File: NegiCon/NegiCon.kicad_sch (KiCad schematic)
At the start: 1 part, among them U4 SC0915

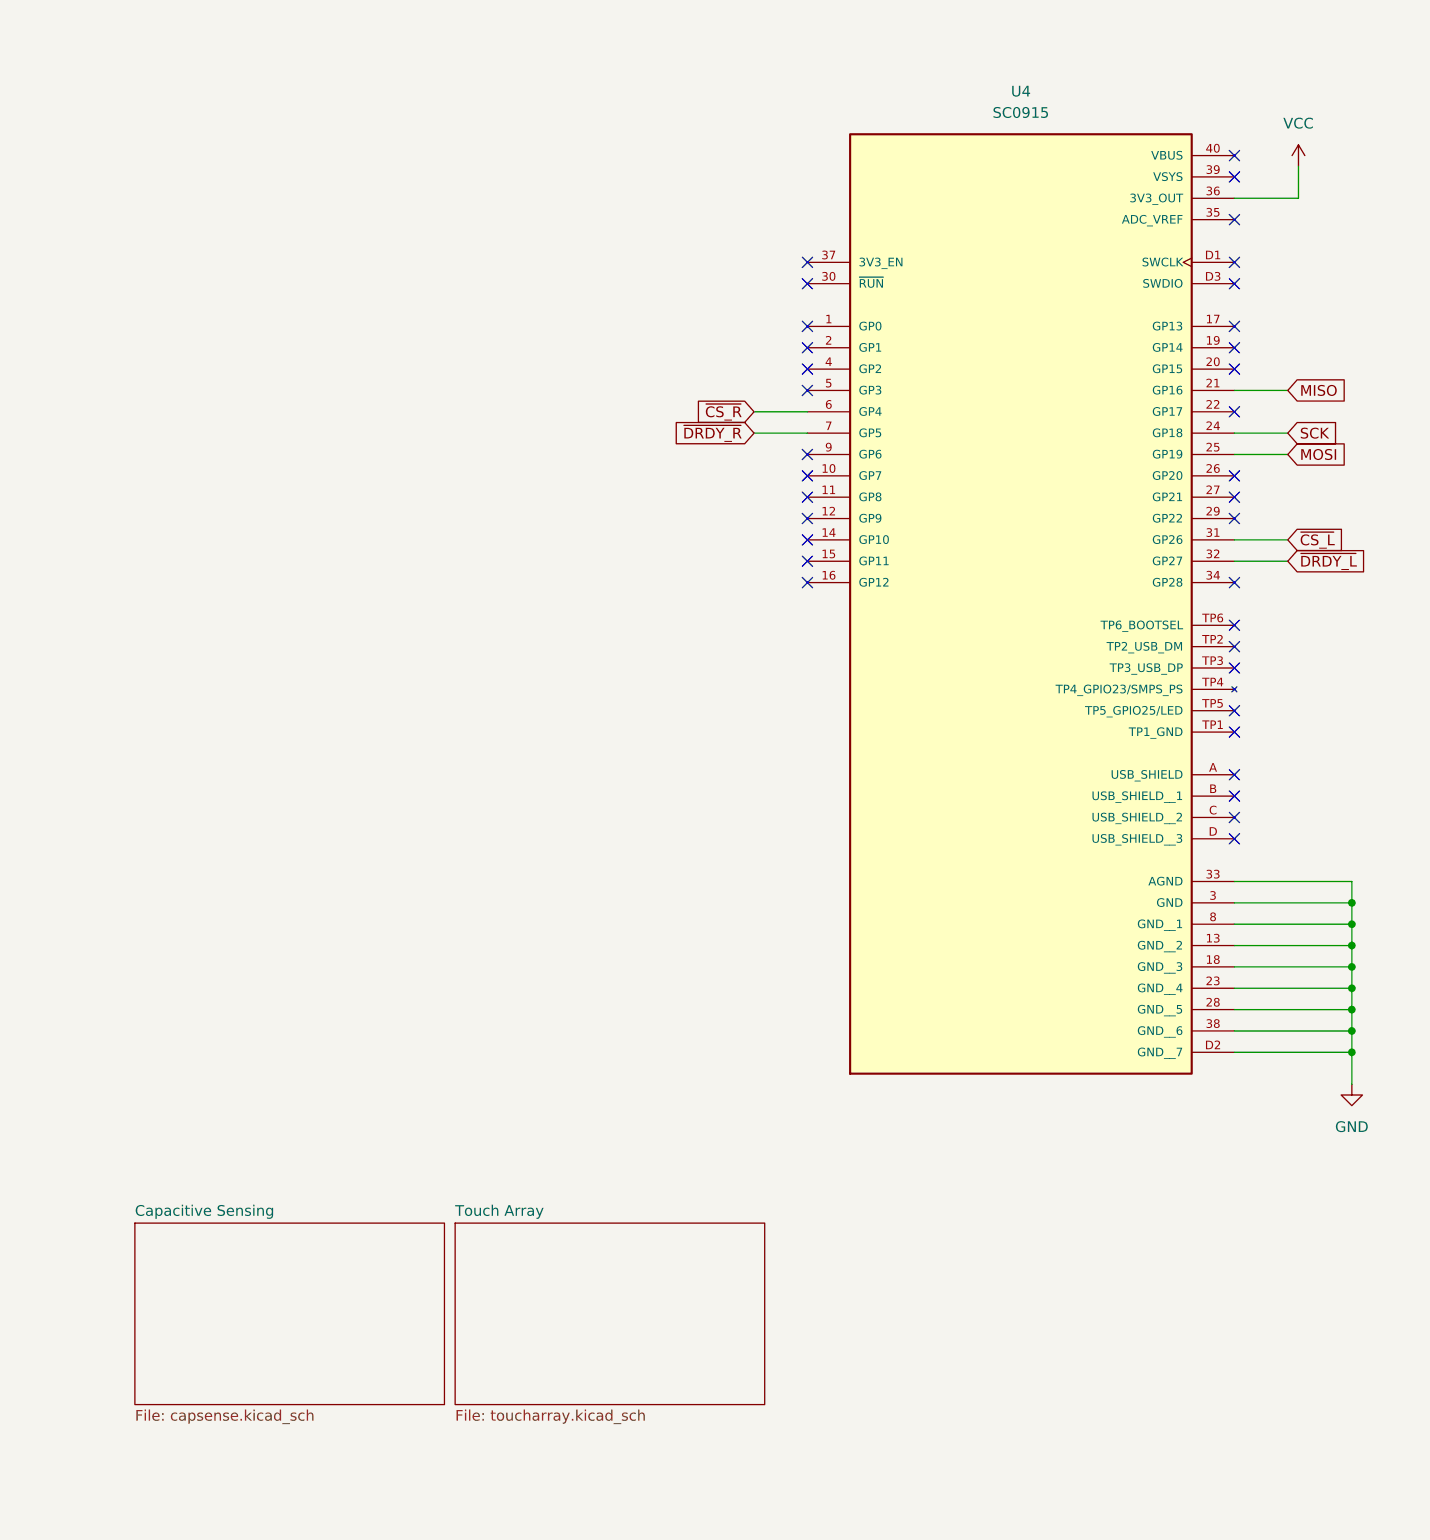
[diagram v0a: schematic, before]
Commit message: add connectors for air sensors
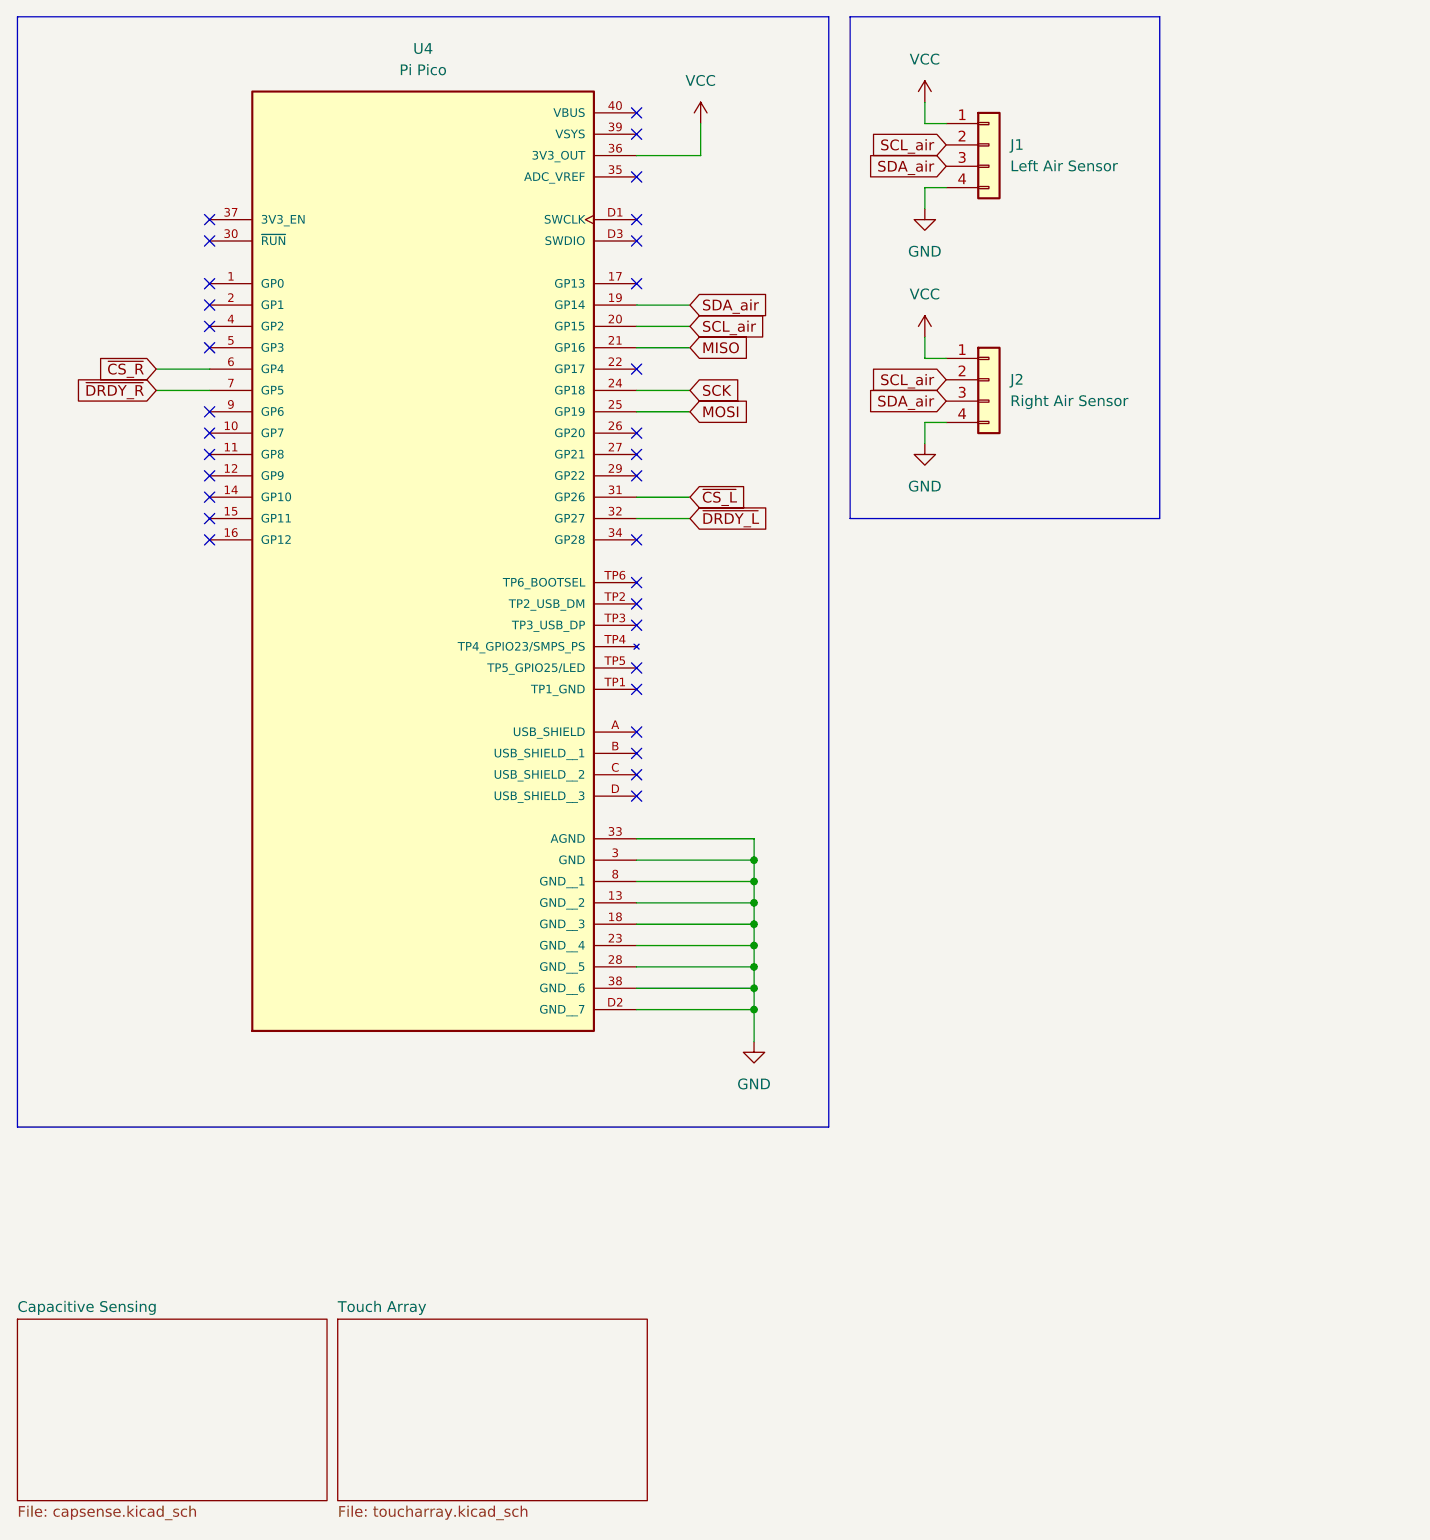
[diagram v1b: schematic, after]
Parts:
- added J1: Left Air Sensor, Connector_Molex:Molex_Nano-Fit_105313-xx04_1x04_P2.50mm_Horizontal, symbol Connector_Generic:Conn_01x04
- added J2: Right Air Sensor, Connector_Molex:Molex_Nano-Fit_105313-xx04_1x04_P2.50mm_Horizontal, symbol Connector_Generic:Conn_01x04
- U4: value SC0915 -> Pi Pico
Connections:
- net GND: now also J1.4 (Pin_4), J2.4 (Pin_4)
- net VCC: now also J1.1 (Pin_1), J2.1 (Pin_1)
- net SDA_air: now reaches U4.19 (GP14)
- net SDA_air: now also J1.3 (Pin_3), J2.3 (Pin_3)
- net SCL_air: now reaches U4.20 (GP15)
- net SCL_air: now also J1.2 (Pin_2), J2.2 (Pin_2)
- no-connect marks 35 -> 33
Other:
- moved on the sheet: U4
